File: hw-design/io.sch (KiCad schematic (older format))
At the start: 12 parts, among them P3 CONN_01X02, P4 CONN_01X03, SW1 SP3T

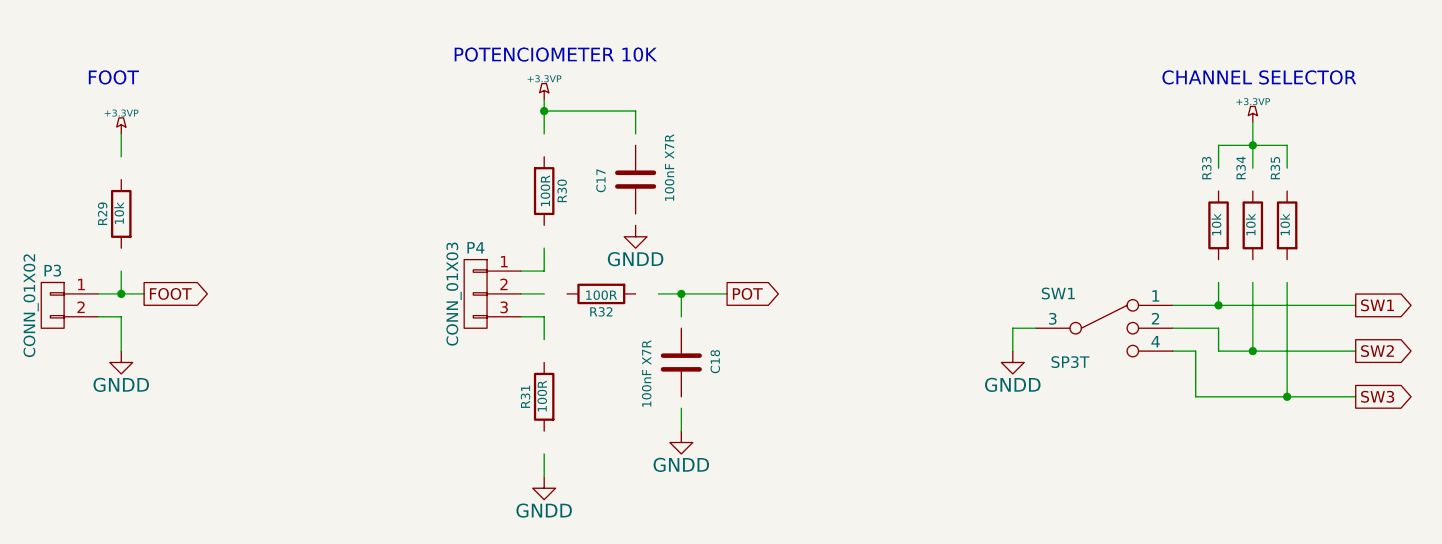
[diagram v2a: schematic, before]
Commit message: adding official kicad library as submodule
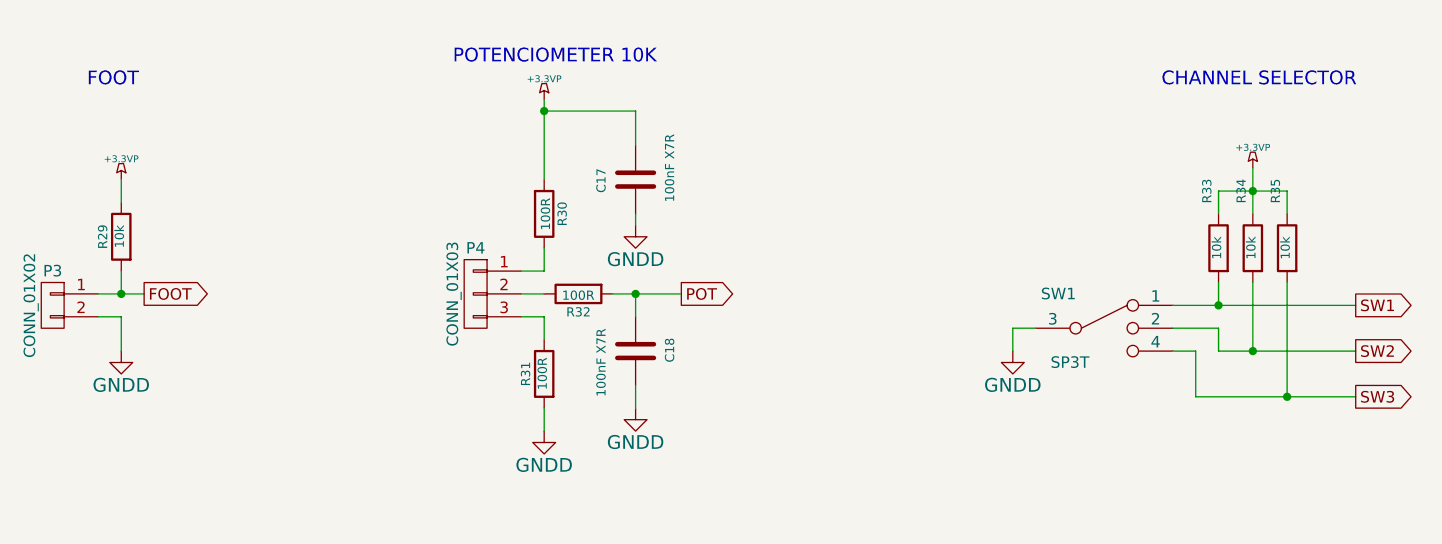
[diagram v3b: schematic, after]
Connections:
- wire segments 33 -> 34
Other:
- moved on the sheet: C18, R29, R30, R31, R32, R33, R34, R35
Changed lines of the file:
@@
 L R R33
 U 1 1 54CBEC23
-P 6850 1850
-F 0 "R33" V 6900 2100 40  0000 C CNN
-F 1 "10k" V 6857 1851 40  0000 C CNN
-F 2 "Resistors_SMD:R_0603" V 6780 1850 30  0001 C CNN
-F 3 "~" H 6850 1850 30  0000 C CNN
-	1    6850 1850
+P 6850 1950
+F 0 "R33" V 6900 2200 40  0000 C CNN
+F 1 "10k" V 6857 1951 40  0000 C CNN
+F 2 "Resistors_SMD:R_0603" V 6780 1950 30  0001 C CNN
+F 3 "~" H 6850 1950 30  0000 C CNN
+	1    6850 1950
 	-1   0    0    -1
 $EndComp
@@
 L R R34
 U 1 1 54CBEC30
-P 7000 1850
-F 0 "R34" V 7050 2100 40  0000 C CNN
-F 1 "10k" V 7007 1851 40  0000 C CNN
-F 2 "Resistors_SMD:R_0603" V 6930 1850 30  0001 C CNN
-F 3 "~" H 7000 1850 30  0000 C CNN
-	1    7000 1850
+P 7000 1950
+F 0 "R34" V 7050 2200 40  0000 C CNN
+F 1 "10k" V 7007 1951 40  0000 C CNN
+F 2 "Resistors_SMD:R_0603" V 6930 1950 30  0001 C CNN
+F 3 "~" H 7000 1950 30  0000 C CNN
+	1    7000 1950
 	-1   0    0    -1
 $EndComp
@@
 L R R35
 U 1 1 54CBEC37
-P 7150 1850
-F 0 "R35" V 7200 2100 40  0000 C CNN
-F 1 "10k" V 7157 1851 40  0000 C CNN
-F 2 "Resistors_SMD:R_0603" V 7080 1850 30  0001 C CNN
-F 3 "~" H 7150 1850 30  0000 C CNN
-	1    7150 1850
+P 7150 1950
+F 0 "R35" V 7200 2200 40  0000 C CNN
+F 1 "10k" V 7157 1951 40  0000 C CNN
+F 2 "Resistors_SMD:R_0603" V 7080 1950 30  0001 C CNN
+F 3 "~" H 7150 1950 30  0000 C CNN
+	1    7150 1950
 	-1   0    0    -1
 $EndComp
@@
 L R R29
 U 1 1 54CBEC53
-P 2050 1800
-F 0 "R29" V 2130 1800 40  0000 C CNN
-F 1 "10k" V 2057 1801 40  0000 C CNN
-F 2 "Resistors_SMD:R_0603" V 1980 1800 30  0001 C CNN
-F 3 "~" H 2050 1800 30  0000 C CNN
-	1    2050 1800
+P 2050 1900
+F 0 "R29" V 2130 1900 40  0000 C CNN
+F 1 "10k" V 2057 1901 40  0000 C CNN
+F 2 "Resistors_SMD:R_0603" V 1980 1900 30  0001 C CNN
+F 3 "~" H 2050 1900 30  0000 C CNN
+	1    2050 1900
 	-1   0    0    -1
 $EndComp
@@
 L R R30
 U 1 1 54CBEC6F
-P 3900 1700
-F 0 "R30" V 3980 1700 40  0000 C CNN
-F 1 "100R" V 3907 1701 40  0000 C CNN
-F 2 "Resistors_SMD:R_0603" V 3830 1700 30  0001 C CNN
-F 3 "~" H 3900 1700 30  0000 C CNN
-	1    3900 1700
+P 3900 1800
+F 0 "R30" V 3980 1800 40  0000 C CNN
+F 1 "100R" V 3907 1801 40  0000 C CNN
+F 2 "Resistors_SMD:R_0603" V 3830 1800 30  0001 C CNN
+F 3 "~" H 3900 1800 30  0000 C CNN
+	1    3900 1800
 	1    0    0    1
 $EndComp
@@
 L R R31
 U 1 1 54CBEC82
-P 3900 2600
-F 0 "R31" V 3980 2600 40  0000 C CNN
-F 1 "100R" V 3907 2601 40  0000 C CNN
-F 2 "Resistors_SMD:R_0603" V 3830 2600 30  0001 C CNN
-F 3 "~" H 3900 2600 30  0000 C CNN
-	1    3900 2600
+P 3900 2500
+F 0 "R31" V 3980 2500 40  0000 C CNN
+F 1 "100R" V 3907 2501 40  0000 C CNN
+F 2 "Resistors_SMD:R_0603" V 3830 2500 30  0001 C CNN
+F 3 "~" H 3900 2500 30  0000 C CNN
+	1    3900 2500
 	-1   0    0    -1
 $EndComp
@@
 L R R32
 U 1 1 54CBEC89
-P 4150 2150
-F 0 "R32" V 4230 2150 40  0000 C CNN
-F 1 "100R" V 4157 2151 40  0000 C CNN
-F 2 "Resistors_SMD:R_0603" V 4080 2150 30  0001 C CNN
-F 3 "~" H 4150 2150 30  0000 C CNN
-	1    4150 2150
+P 4050 2150
+F 0 "R32" V 4130 2150 40  0000 C CNN
+F 1 "100R" V 4057 2151 40  0000 C CNN
+F 2 "Resistors_SMD:R_0603" V 3980 2150 30  0001 C CNN
+F 3 "~" H 4050 2150 30  0000 C CNN
+	1    4050 2150
 	0    -1   1    0
 $EndComp
-Text GLabel 4700 2150 2    50   Output ~ 0
+Text GLabel 4500 2150 2    50   Output ~ 0
 POT
 $Comp
 L C C18
 U 1 1 54CBEC99
-P 4500 2450
-F 0 "C18" V 4350 2400 40  0000 L CNN
-F 1 "100nF X7R" V 4650 2250 40  0000 L CNN
-F 2 "Capacitors_SMD:C_0603" H 4538 2300 30  0001 C CNN
-F 3 "~" H 4500 2450 60  0000 C CNN
-	1    4500 2450
+P 4300 2400
+F 0 "C18" V 4150 2350 40  0000 L CNN
+F 1 "100nF X7R" V 4450 2200 40  0000 L CNN
+F 2 "Capacitors_SMD:C_0603" H 4338 2250 30  0001 C CNN
+F 3 "~" H 4300 2400 60  0000 C CNN
+	1    4300 2400
 	-1   0    0    -1
 $EndComp
@@
 L +3.3VP #PWR061
 U 1 1 54E65255
-P 2050 1450
-F 0 "#PWR061" H 2100 1480 20  0001 C CNN
-F 1 "+3.3VP" H 2050 1540 30  0000 C CNN
-F 2 "" H 2050 1450 60  0000 C CNN
-F 3 "" H 2050 1450 60  0000 C CNN
-	1    2050 1450
+P 2050 1650
+F 0 "#PWR061" H 2100 1680 20  0001 C CNN
+F 1 "+3.3VP" H 2050 1740 30  0000 C CNN
+F 2 "" H 2050 1650 60  0000 C CNN
+F 3 "" H 2050 1650 60  0000 C CNN
+	1    2050 1650
 	1    0    0    -1
 $EndComp
@@
 L GNDD #PWR062
 U 1 1 54E661EA
-P 3900 2950
-F 0 "#PWR062" H 3900 2700 60  0001 C CNN
-F 1 "GNDD" H 3900 2800 60  0000 C CNN
-F 2 "" H 3900 2950 60  0000 C CNN
-F 3 "" H 3900 2950 60  0000 C CNN
-	1    3900 2950
+P 3900 2750
+F 0 "#PWR062" H 3900 2500 60  0001 C CNN
+F 1 "GNDD" H 3900 2600 60  0000 C CNN
+F 2 "" H 3900 2750 60  0000 C CNN
+F 3 "" H 3900 2750 60  0000 C CNN
+	1    3900 2750
 	1    0    0    -1
 $EndComp
@@
 L GNDD #PWR063
 U 1 1 54E665CD
-P 4500 2750
-F 0 "#PWR063" H 4500 2500 60  0001 C CNN
-F 1 "GNDD" H 4500 2600 60  0000 C CNN
-F 2 "" H 4500 2750 60  0000 C CNN
-F 3 "" H 4500 2750 60  0000 C CNN
-	1    4500 2750
+P 4300 2650
+F 0 "#PWR063" H 4300 2400 60  0001 C CNN
+F 1 "GNDD" H 4300 2500 60  0000 C CNN
+F 2 "" H 4300 2650 60  0000 C CNN
+F 3 "" H 4300 2650 60  0000 C CNN
+	1    4300 2650
 	1    0    0    -1
 $EndComp
@@
 L +3.3VP #PWR066
 U 1 1 54E69C36
-P 7000 1400
-F 0 "#PWR066" H 7050 1430 20  0001 C CNN
-F 1 "+3.3VP" H 7000 1490 30  0000 C CNN
-F 2 "" H 7000 1400 60  0000 C CNN
-F 3 "" H 7000 1400 60  0000 C CNN
-	1    7000 1400
+P 7000 1600
+F 0 "#PWR066" H 7050 1630 20  0001 C CNN
+F 1 "+3.3VP" H 7000 1690 30  0000 C CNN
+F 2 "" H 7000 1600 60  0000 C CNN
+F 3 "" H 7000 1600 60  0000 C CNN
+	1    7000 1600
 	1    0    0    -1
 $EndComp
@@
 	5950 2300 5950 2400
 Wire Wire Line
-	7150 1500 7150 1600
-Wire Wire Line
-	6850 1500 7150 1500
-Wire Wire Line
-	6850 1500 6850 1600
-Wire Wire Line
-	7000 1400 7000 1600
-Connection ~ 7000 1500
+	7150 1700 7150 1800
+Wire Wire Line
+	6850 1700 7150 1700
+Wire Wire Line
+	6850 1700 6850 1800
+Wire Wire Line
+	7000 1600 7000 1800
+Connection ~ 7000 1700
 Wire Wire Line
 	6650 2200 7450 2200
@@
 	1950 2150 2150 2150
 Wire Wire Line
-	2050 1450 2050 1550
+	2050 1650 2050 1750
 Connection ~ 2050 2150
 Wire Wire Line
-	3900 2850 3900 2950
+	3900 2650 3900 2750
 Wire Wire Line
 	3800 2250 3900 2250
@@
 	3900 2050 3900 1950
 Wire Wire Line
-	4400 2150 4700 2150
-Wire Wire Line
-	4500 2750 4500 2650
-Wire Wire Line
-	4500 2150 4500 2250
-Connection ~ 4500 2150
+	4200 2150 4500 2150
+Wire Wire Line
+	4300 2650 4300 2550
+Wire Wire Line
+	4300 2150 4300 2250
+Connection ~ 4300 2150
 Wire Wire Line
 	2050 2250 2050 2400
 Wire Wire Line
-	3900 1300 3900 1450
-Wire Wire Line
-	4300 1450 4300 1350
+	3900 1300 3900 1650
+Wire Wire Line
+	4300 1500 4300 1350
 Wire Wire Line
 	4300 1350 3900 1350
@@
 Wire Wire Line
 	6750 2400 6650 2400
+Wire Wire Line
+	4300 1800 4300 1850
 $EndSCHEMATC

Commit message: sch: updating some cached symbols
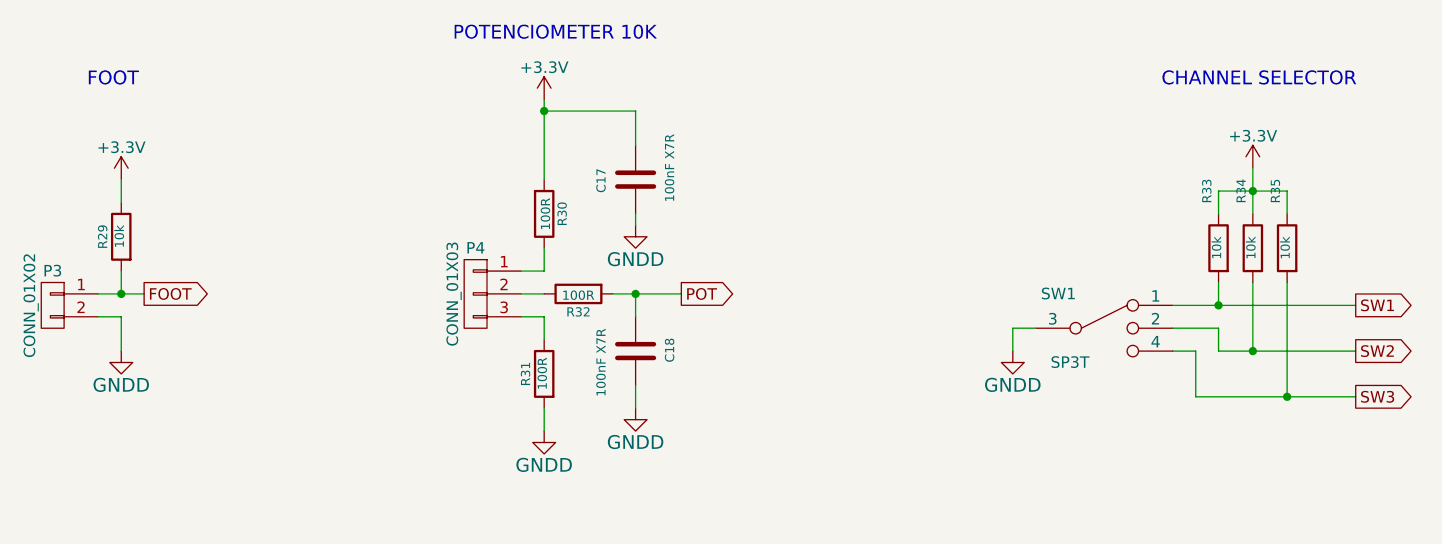
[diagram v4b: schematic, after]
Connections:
- net +3.3VP renamed +3V3
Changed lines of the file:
@@
 LIBS:conn
 LIBS:interface
-LIBS:expression-pedal-cache
 EELAYER 25 0
 EELAYER END
@@
 	-1   0    0    -1
 $EndComp
-Text Notes 3500 1150 0    60   ~ 0
+Text Notes 3500 1050 0    60   ~ 0
 POTENCIOMETER 10K
 Text Notes 6600 1250 0    60   ~ 0
@@
 $EndComp
 $Comp
-L +3.3VP #PWR061
-U 1 1 54E65255
-P 2050 1650
-F 0 "#PWR061" H 2100 1680 20  0001 C CNN
-F 1 "+3.3VP" H 2050 1740 30  0000 C CNN
-F 2 "" H 2050 1650 60  0000 C CNN
-F 3 "" H 2050 1650 60  0000 C CNN
-	1    2050 1650
-	1    0    0    -1
-$EndComp
-$Comp
 L GNDD #PWR062
 U 1 1 54E661EA
@@
 $EndComp
 $Comp
-L +3.3VP #PWR064
-U 1 1 54E66A75
-P 3900 1300
-F 0 "#PWR064" H 3950 1330 20  0001 C CNN
-F 1 "+3.3VP" H 3900 1390 30  0000 C CNN
-F 2 "" H 3900 1300 60  0000 C CNN
-F 3 "" H 3900 1300 60  0000 C CNN
-	1    3900 1300
-	1    0    0    -1
-$EndComp
-$Comp
 L GNDD #PWR065
 U 1 1 54E66D8A
@@
 $EndComp
 $Comp
-L +3.3VP #PWR066
-U 1 1 54E69C36
-P 7000 1600
-F 0 "#PWR066" H 7050 1630 20  0001 C CNN
-F 1 "+3.3VP" H 7000 1690 30  0000 C CNN
-F 2 "" H 7000 1600 60  0000 C CNN
-F 3 "" H 7000 1600 60  0000 C CNN
-	1    7000 1600
-	1    0    0    -1
-$EndComp
-$Comp
 L CONN_01X02 P3
 U 1 1 54E6B5CA
@@
 Wire Wire Line
 	4300 1800 4300 1850
+$Comp
+L +3.3V #PWR?
+U 1 1 556F3C3C
+P 2050 1650
+F 0 "#PWR?" H 2050 1500 50  0001 C CNN
+F 1 "+3.3V" H 2050 1790 50  0000 C CNN
+F 2 "" H 2050 1650 60  0000 C CNN
+F 3 "" H 2050 1650 60  0000 C CNN
+	1    2050 1650
+	1    0    0    -1
+$EndComp
+$Comp
+L +3.3V #PWR?
+U 1 1 556F3CC5
+P 3900 1300
+F 0 "#PWR?" H 3900 1150 50  0001 C CNN
+F 1 "+3.3V" H 3900 1440 50  0000 C CNN
+F 2 "" H 3900 1300 60  0000 C CNN
+F 3 "" H 3900 1300 60  0000 C CNN
+	1    3900 1300
+	1    0    0    -1
+$EndComp
+$Comp
+L +3.3V #PWR?
+U 1 1 556F428C
+P 7000 1600
+F 0 "#PWR?" H 7000 1450 50  0001 C CNN
+F 1 "+3.3V" H 7000 1740 50  0000 C CNN
+F 2 "" H 7000 1600 60  0000 C CNN
+F 3 "" H 7000 1600 60  0000 C CNN
+	1    7000 1600
+	1    0    0    -1
+$EndComp
 $EndSCHEMATC
